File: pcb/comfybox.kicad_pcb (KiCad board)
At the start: 2 copper layers, 240 x 130 mm, 20 parts, among them K1 SW_CHOC, K2 SW_CHOC, K3 SW_CHOC, K4 SW_CHOC, P1 SW_CHOC, P2 SW_CHOC, P3 SW_CHOC, P4 SW_CHOC

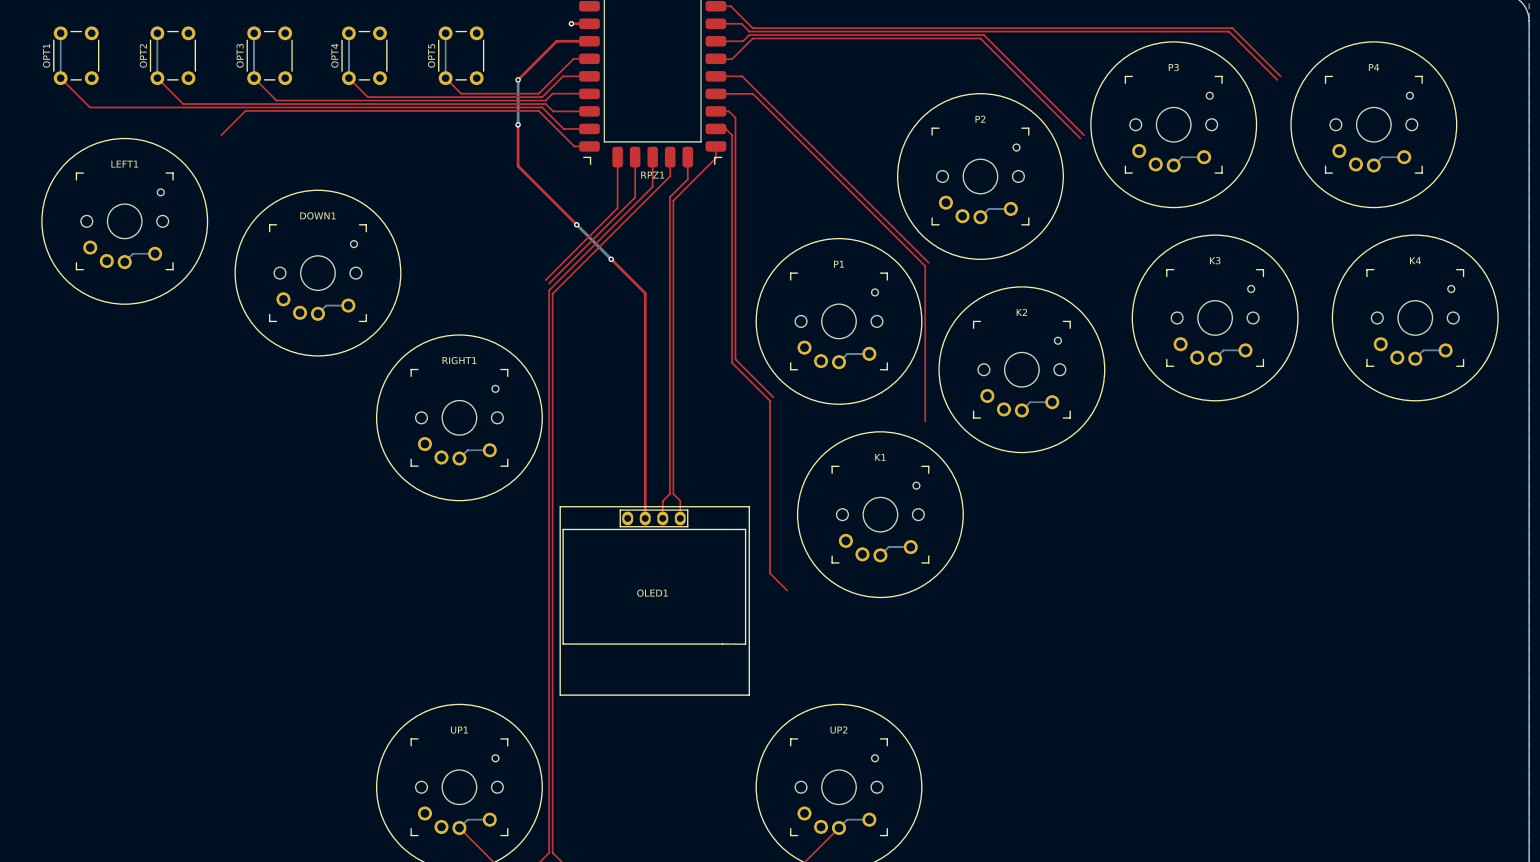
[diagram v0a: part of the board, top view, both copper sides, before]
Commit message: layout adjustments and MX compatibility
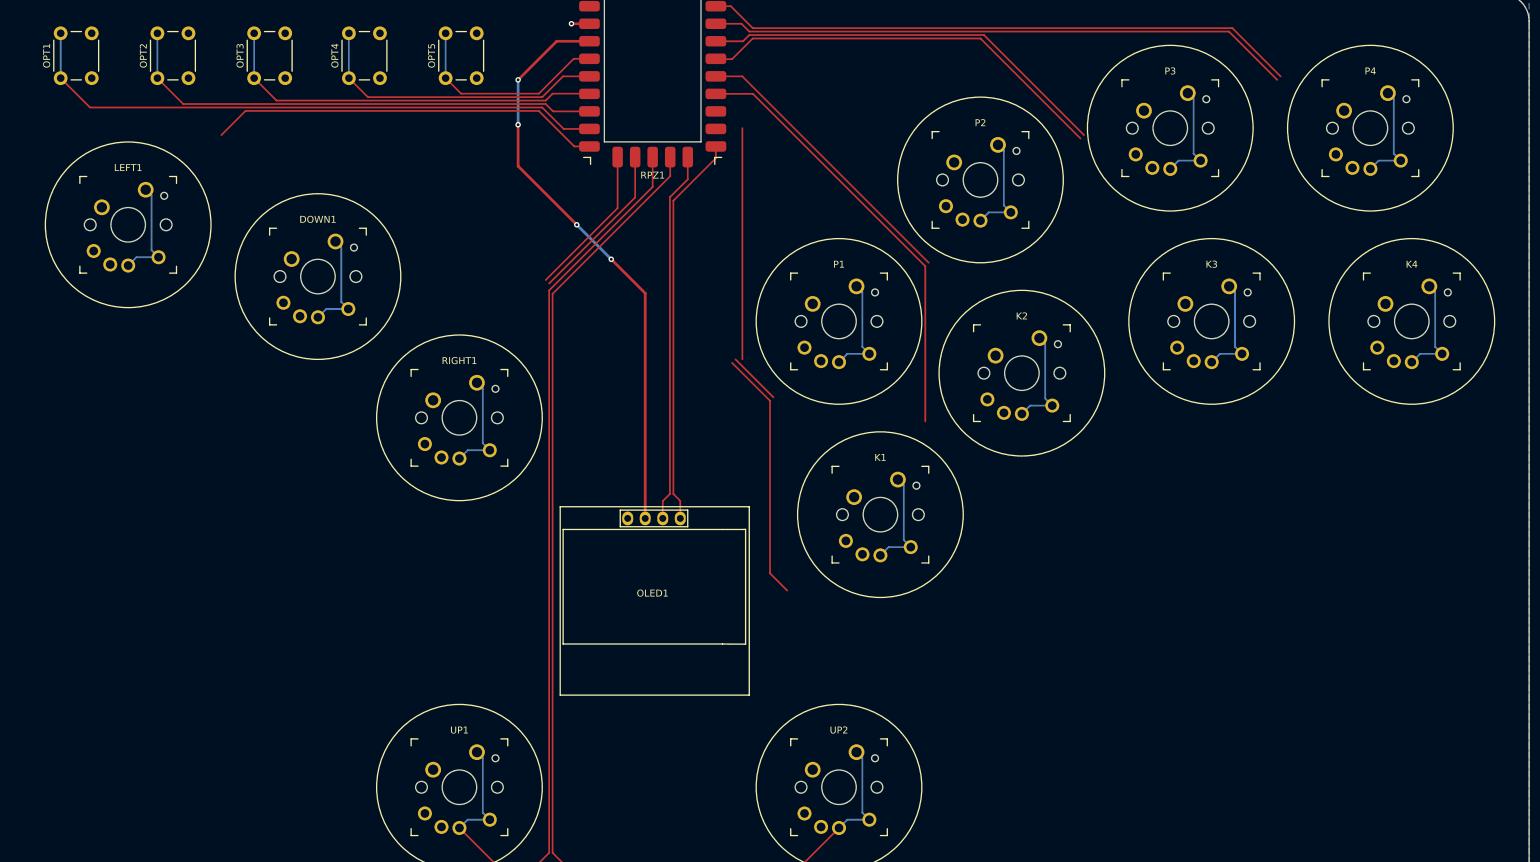
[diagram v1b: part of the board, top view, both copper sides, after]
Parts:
- DOWN1, K1, K2, K3, K4, LEFT1, P1, P2, P3, P4, RIGHT1, UP1, UP2: footprint Switch:Kailh_PG1350_Gateron_KS27_KS33 -> Switch:Kailh_PG1350_Gateron_KS33_MX
- moved K3 0.71 mm to (216.0, 70.5)
- moved K4 0.71 mm to (245.0, 70.5)
- moved P3 0.71 mm to (210.0, 42.5)
- moved P4 0.71 mm to (239.0, 42.5)
- moved LEFT1 0.71 mm to (59.0, 56.5)
- moved DOWN1 0.50 mm to (86.5, 64.0)
- moved K2 0.50 mm to (188.5, 78.0)
- moved P2 0.50 mm to (182.5, 50.0)
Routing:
- net K1: track 76.9 -> 51.8 mm
- net P4: track 91.0 -> 101.5 mm
- net UP R: track 157.5 -> 168.0 mm
- net UP L: track 128.1 -> 138.6 mm
- net K3: track 65.0 -> 75.6 mm
- net K2: track 68.1 -> 78.6 mm
- net RIGHT: track 28.4 -> 38.9 mm
- net LEFT: track 61.8 -> 72.4 mm
- net P3: track 64.6 -> 75.2 mm
- net K4: track 89.6 -> 100.2 mm
- net DOWN: track 27.1 -> 37.7 mm
- net P2: track 46.9 -> 57.5 mm
- net P1: track 50.9 -> 56.7 mm

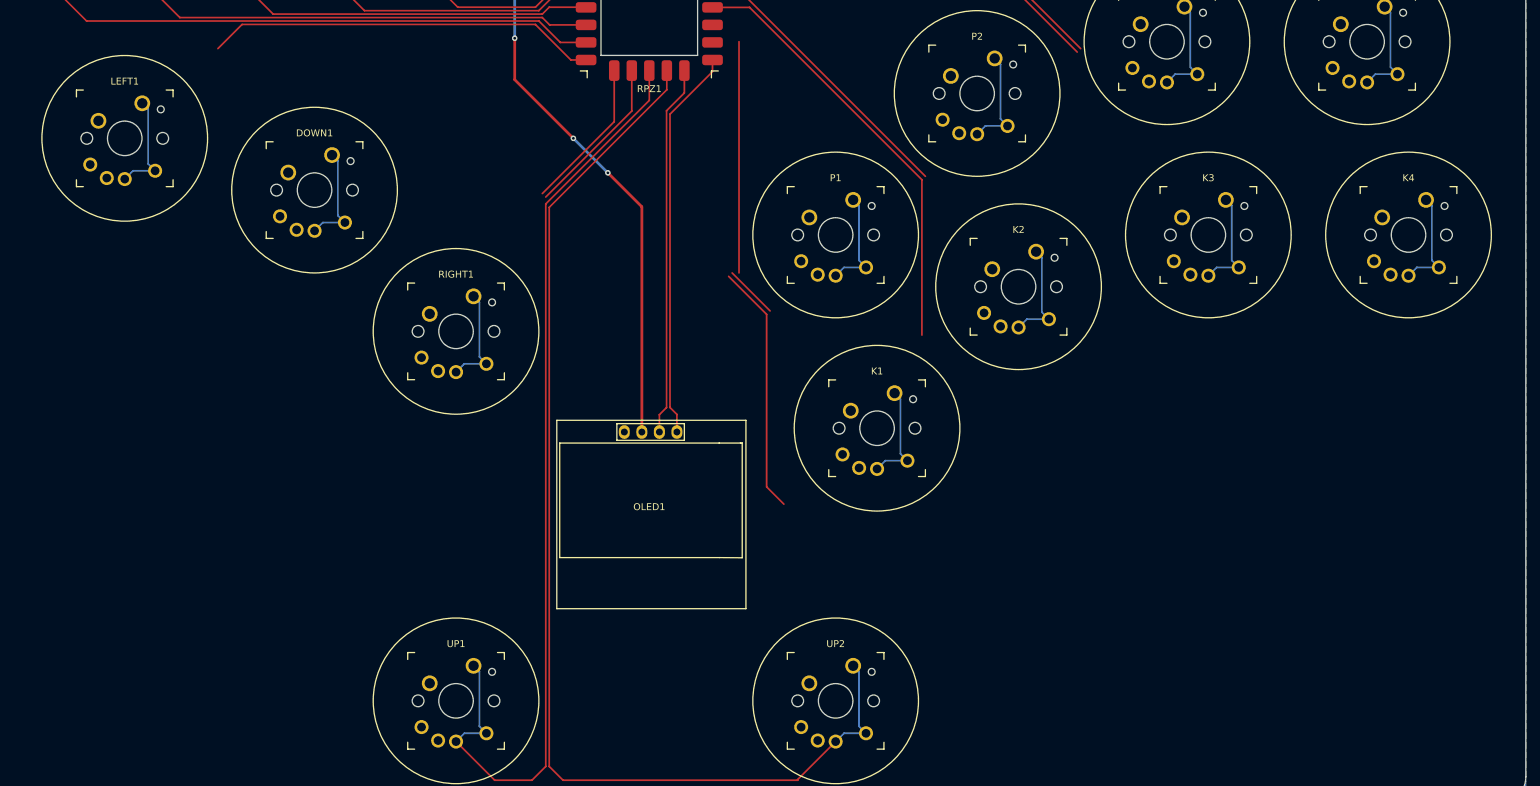
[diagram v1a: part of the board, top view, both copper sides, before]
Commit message: add logo and update to kicad7
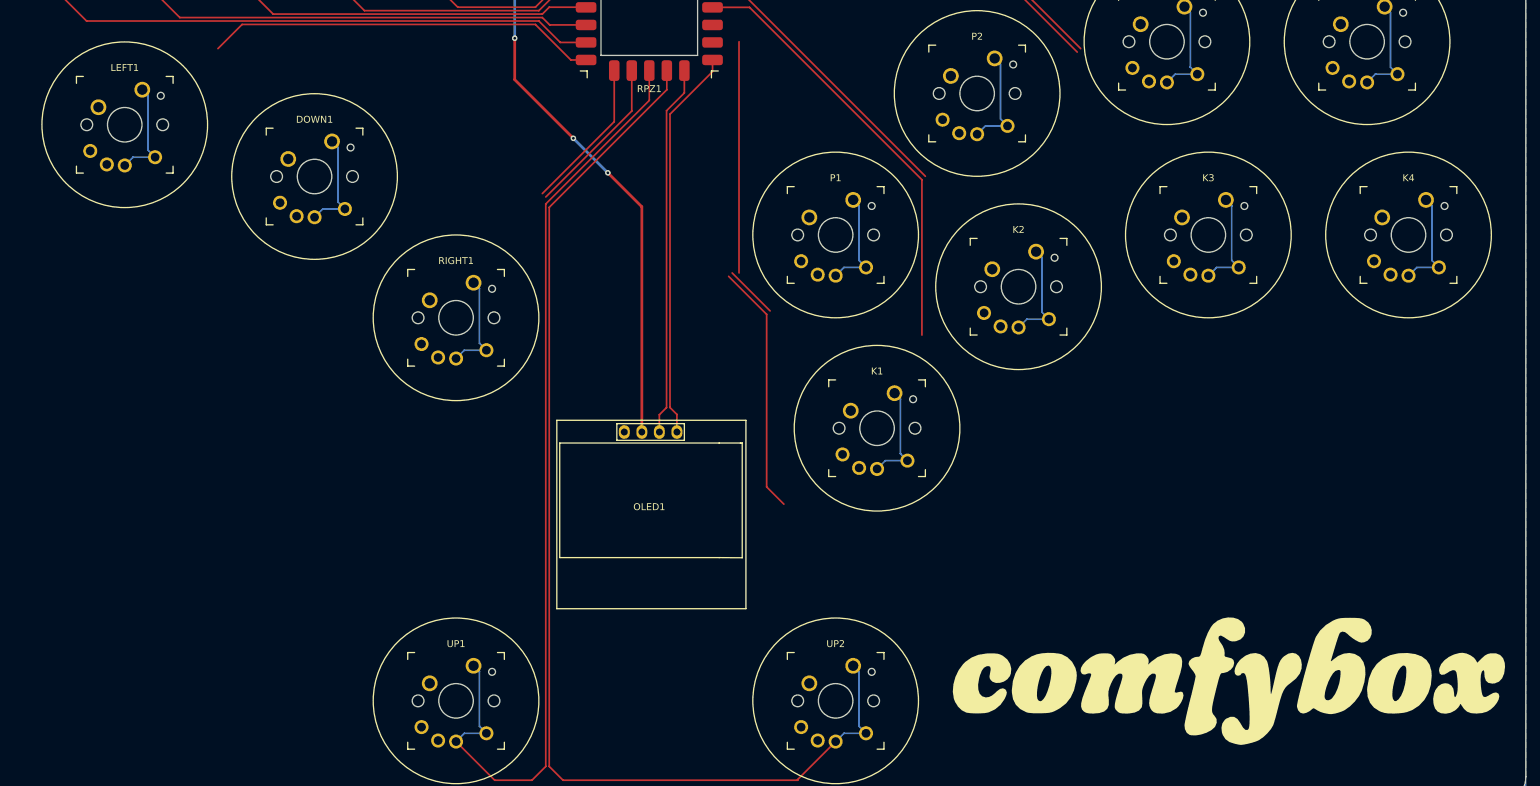
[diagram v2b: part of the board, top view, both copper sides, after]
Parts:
- added G***: LOGO, LOGO, F.Cu at (219.0, 135.0)
- moved DOWN1 1.97 mm to (86.5, 62.0)
- moved LEFT1 1.97 mm to (59.0, 54.5)
- moved RIGHT1 1.97 mm to (107.0, 82.5)

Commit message: redo traces
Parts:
- moved G*** 2.50 mm to (216.5, 135.0)
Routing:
- net K4: track 100.2 -> 162.8 mm
- net K3: track 75.6 -> 129.2 mm
- net K1: track 51.8 -> 101.9 mm
- net DOWN: track 37.7 -> 67.1 mm
- net K2: track 78.6 -> 96.7 mm
- net RIGHT: track 38.9 -> 55.7 mm
- net P4: track 101.5 -> 118.0 mm
- net LEFT: track 72.4 -> 85.8 mm
- net P3: track 75.2 -> 87.7 mm
- net P2: track 57.5 -> 66.7 mm
- net P1: track 56.7 -> 53.3 mm
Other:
- board text added: "Rev ${REVISION}"
